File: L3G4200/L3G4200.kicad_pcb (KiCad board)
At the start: 2 copper layers, 25.4 x 17.8 mm, 30 parts, among them J1 Conn_01x06, J2 Conn_01x04, J3 Conn_01x06, J4 Conn_01x04, Q1 BSS138DW, Q2 BSS138DW, U1 AP2127K-3.3, U2 L3G4200

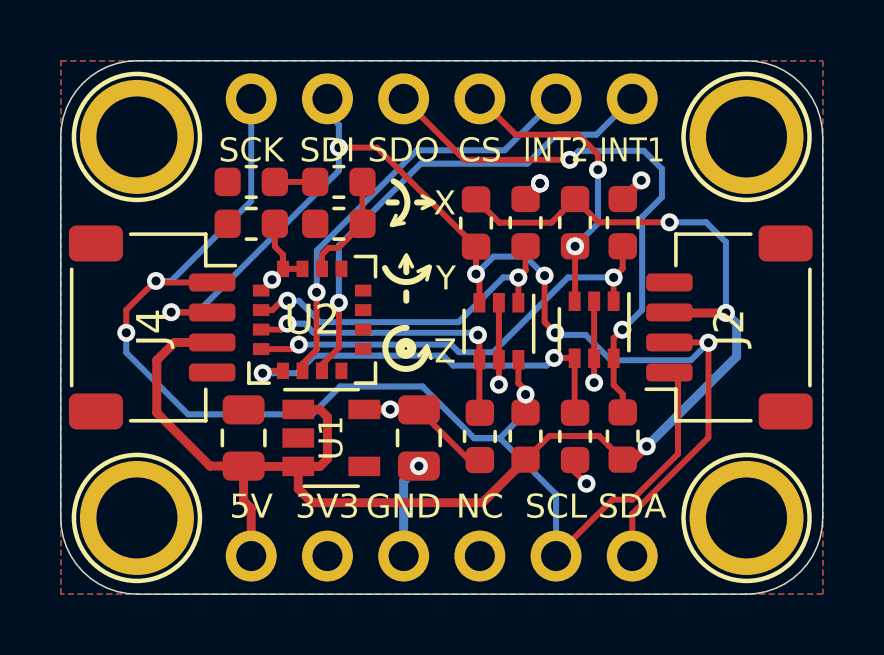
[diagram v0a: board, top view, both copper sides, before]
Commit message: Copper Pour Edits
Copper pour reduced to have 0.2mm edge clearance
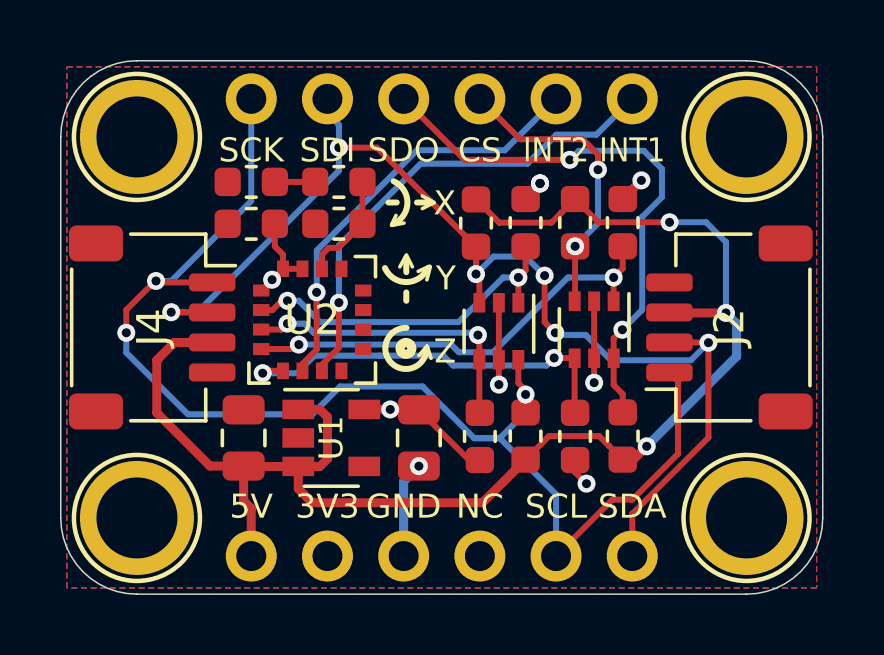
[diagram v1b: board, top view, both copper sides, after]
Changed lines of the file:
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@@
   )
   (setup
-    (last_trace_width 0.2)
+    (last_trace_width 0.127)
     (user_trace_width 0.2)
     (user_trace_width 0.25)
@@
   (segment (start 61.849 35.1409) (end 61.849 33.2359) (width 0.2) (layer B.Cu) (net 5))
   (segment (start 61.849 33.2359) (end 64.5795 30.5054) (width 0.2) (layer B.Cu) (net 5))
-  (segment (start 66.421 33.2741) (end 66.421 34.1884) (width 0.2) (layer F.Cu) (net 8))
-  (segment (start 66.533 34.3004) (end 66.533 35.1434) (width 0.2) (layer F.Cu) (net 8))
-  (segment (start 66.421 34.1884) (end 66.533 34.3004) (width 0.2) (layer F.Cu) (net 8))
-  (segment (start 68.072 33.2614) (end 68.072 34.0614) (width 0.2) (layer F.Cu) (net 9))
-  (segment (start 67.833 34.3004) (end 67.833 35.1434) (width 0.2) (layer F.Cu) (net 9))
-  (segment (start 68.072 34.0614) (end 67.833 34.3004) (width 0.2) (layer F.Cu) (net 9))
   (segment (start 67.833 37.0434) (end 67.833 37.8229) (width 0.2) (layer F.Cu) (net 6))
   (segment (start 68.072 38.0619) (end 68.072 38.7984) (width 0.2) (layer F.Cu) (net 6))
@@
   (segment (start 66.4083 36.1442) (end 66.4845 36.2204) (width 0.2) (layer B.Cu) (net 7))
   (segment (start 62.9412 36.1442) (end 66.4083 36.1442) (width 0.2) (layer B.Cu) (net 7))
+  (segment (start 66.421 33.2741) (end 66.421 34.1884) (width 0.2) (layer F.Cu) (net 8))
+  (segment (start 66.533 34.3004) (end 66.533 35.1434) (width 0.2) (layer F.Cu) (net 8))
+  (segment (start 66.421 34.1884) (end 66.533 34.3004) (width 0.2) (layer F.Cu) (net 8))
   (segment (start 66.421 34.1884) (end 66.421 34.1884) (width 0.2) (layer F.Cu) (net 8))
   (via (at 66.421 34.1884) (size 0.6) (drill 0.3) (layers F.Cu B.Cu) (net 8))
@@
   (segment (start 63.1189 29.972) (end 61.849 29.972) (width 0.2) (layer F.Cu) (net 8))
   (segment (start 66.421 33.2741) (end 63.1189 29.972) (width 0.2) (layer F.Cu) (net 8))
+  (segment (start 68.072 33.2614) (end 68.072 34.0614) (width 0.2) (layer F.Cu) (net 9))
+  (segment (start 67.833 34.3004) (end 67.833 35.1434) (width 0.2) (layer F.Cu) (net 9))
+  (segment (start 68.072 34.0614) (end 67.833 34.3004) (width 0.2) (layer F.Cu) (net 9))
   (via (at 60.1345 35.0774) (size 0.6) (drill 0.3) (layers F.Cu B.Cu) (net 9))
   (segment (start 59.944 35.0774) (end 60.1345 35.0774) (width 0.2) (layer F.Cu) (net 9))
@@
   (segment (start 60.1345 35.0774) (end 60.5155 35.0774) (width 0.2) (layer B.Cu) (net 9))
   (segment (start 60.5155 35.0774) (end 61.2267 35.7886) (width 0.2) (layer B.Cu) (net 9))
-  (segment (start 71.008 36.9926) (end 71.008 37.8864) (width 0.2) (layer F.Cu) (net 16))
-  (segment (start 71.3105 38.1889) (end 71.3105 38.7984) (width 0.2) (layer F.Cu) (net 16))
-  (segment (start 71.008 37.8864) (end 71.3105 38.1889) (width 0.2) (layer F.Cu) (net 16))
-  (segment (start 71.3105 33.2614) (end 71.3105 33.9979) (width 0.2) (layer F.Cu) (net 17))
-  (segment (start 71.008 34.3004) (end 71.008 35.0926) (width 0.2) (layer F.Cu) (net 17))
-  (segment (start 71.3105 33.9979) (end 71.008 34.3004) (width 0.2) (layer F.Cu) (net 17))
   (segment (start 69.723 35.0776) (end 69.708 35.0926) (width 0.2) (layer F.Cu) (net 10))
   (segment (start 69.723 33.2614) (end 69.723 35.0776) (width 0.2) (layer F.Cu) (net 10))
@@
   (segment (start 70.485 32.4994) (end 69.723 33.2614) (width 0.2) (layer B.Cu) (net 10))
   (segment (start 70.485 30.2006) (end 70.485 30.7086) (width 0.2) (layer F.Cu) (net 10))
-  (segment (start 69.8246 29.5402) (end 70.485 30.2006) (width 0.2) (layer F.Cu) (net 10))
-  (segment (start 66.548 28.3464) (end 67.7418 29.5402) (width 0.2) (layer F.Cu) (net 10))
-  (segment (start 67.7418 29.5402) (end 69.8246 29.5402) (width 0.2) (layer F.Cu) (net 10))
+  (segment (start 69.977 29.6926) (end 70.485 30.2006) (width 0.2) (layer F.Cu) (net 10))
+  (segment (start 66.548 28.3464) (end 67.8942 29.6926) (width 0.2) (layer F.Cu) (net 10))
+  (segment (start 67.8942 29.6926) (end 69.977 29.6926) (width 0.2) (layer F.Cu) (net 10))
   (segment (start 69.708 38.7961) (end 69.723 38.8111) (width 0.2) (layer F.Cu) (net 11))
   (segment (start 69.708 36.9926) (end 69.708 38.7961) (width 0.2) (layer F.Cu) (net 11))
@@
   (segment (start 61.1124 34.790201) (end 61.1124 33.4772) (width 0.2) (layer B.Cu) (net 15))
   (segment (start 61.106503 34.796098) (end 61.1124 34.790201) (width 0.2) (layer B.Cu) (net 15))
+  (segment (start 71.008 36.9926) (end 71.008 37.8864) (width 0.2) (layer F.Cu) (net 16))
+  (segment (start 71.3105 38.1889) (end 71.3105 38.7984) (width 0.2) (layer F.Cu) (net 16))
+  (segment (start 71.008 37.8864) (end 71.3105 38.1889) (width 0.2) (layer F.Cu) (net 16))
   (via (at 71.2978 36.0426) (size 0.6) (drill 0.3) (layers F.Cu B.Cu) (net 16))
   (segment (start 71.008 36.9926) (end 71.008 36.3324) (width 0.2) (layer F.Cu) (net 16))
@@
   (segment (start 71.9582 35.3822) (end 71.2978 36.0426) (width 0.2) (layer B.Cu) (net 16))
   (segment (start 71.9582 32.2834) (end 71.9582 35.3822) (width 0.2) (layer B.Cu) (net 16))
+  (segment (start 71.3105 33.2614) (end 71.3105 33.9979) (width 0.2) (layer F.Cu) (net 17))
+  (segment (start 71.008 34.3004) (end 71.008 35.0926) (width 0.2) (layer F.Cu) (net 17))
+  (segment (start 71.3105 33.9979) (end 71.008 34.3004) (width 0.2) (layer F.Cu) (net 17))
   (via (at 60.5155 36.5379) (size 0.6) (drill 0.3) (layers F.Cu B.Cu) (net 17))
   (segment (start 59.26 36.6874) (end 60.366 36.6874) (width 0.2) (layer F.Cu) (net 17))
@@
     (polygon
       (pts
-        (xy 52.578 27.0764) (xy 77.978 27.0764) (xy 77.978 44.8564) (xy 52.578 44.8564)
+        (xy 52.7812 27.2796) (xy 77.7748 27.2796) (xy 77.7748 44.6532) (xy 52.7812 44.6532)
       )
     )
@@
     (polygon
       (pts
-        (xy 52.578 27.0764) (xy 77.978 27.0764) (xy 77.978 44.8564) (xy 52.578 44.8564)
+        (xy 52.7812 27.2796) (xy 77.7748 27.2796) (xy 77.7748 44.6532) (xy 52.7812 44.6532)
       )
     )

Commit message: Soldermask width adjusted
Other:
- rule solder_mask_min_width: 0.1 -> 0.05
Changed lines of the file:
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@@
     (pad_drill 1)
     (pad_to_mask_clearance 0)
-    (solder_mask_min_width 0.1)
+    (solder_mask_min_width 0.05)
     (aux_axis_origin 0 0)
     (visible_elements 7FFFFFFF)
